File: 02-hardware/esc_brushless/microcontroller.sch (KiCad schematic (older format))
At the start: 0 parts

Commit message: Schematics v1.0 - Architecture, MOS power stage, mos driver stage and RS485 interface
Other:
- note added: "1 I2C"
- note added: "1 SPI"
- note added: "1 input capture"
- note added: "2 UART"
- note added: "4 GPIO input"
- note added: "5 GPIO output"
- note added: "6 timer channels"
- note added: "ADC 7 channels"
- note added: "SWD"
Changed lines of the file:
@@
 $Descr A4 11693 8268
 encoding utf-8
-Sheet 3 5
+Sheet 4 7
 Title "ESC Brushless - Microcontroller"
 Date "2021-02-09"
@@
 Comment4 ""
 $EndDescr
+Text HLabel 2150 5150 0    50   Input ~ 0
+\OVR_CUR_FLT
+Text HLabel 2150 5250 0    50   Input ~ 0
+\FLT
+Text HLabel 950  1600 0    50   UnSpc ~ 0
+3.3V_MCU
+Text HLabel 2150 5050 0    50   Input ~ 0
+\PWRGD_FLT
+Text HLabel 2150 3550 0    50   Output ~ 0
+SPI_CS
+Text HLabel 2150 3650 0    50   Output ~ 0
+SPI_MOSI
+Text HLabel 2150 3850 0    50   Output ~ 0
+SPI_CLK
+Text HLabel 2150 3750 0    50   Input ~ 0
+SPI_MISO
+Text HLabel 2150 4150 0    50   Output ~ 0
+INH_A
+Text HLabel 2150 4250 0    50   Output ~ 0
+INL_A
+Text HLabel 2150 4350 0    50   Output ~ 0
+INH_B
+Text HLabel 2150 4450 0    50   Output ~ 0
+INL_B
+Text HLabel 2150 4550 0    50   Output ~ 0
+INH_C
+Text HLabel 2150 4650 0    50   Output ~ 0
+INL_C
+Text HLabel 2150 1150 0    50   Input ~ 0
+SO1
+Text HLabel 1000 1450 0    50   UnSpc ~ 0
+REF
+Text HLabel 2150 1250 0    50   Input ~ 0
+SO2
+Text HLabel 2150 5700 0    50   Output ~ 0
+DC_CAL
+Text HLabel 2150 5600 0    50   Output ~ 0
+EN_GATE
+Text HLabel 2150 1050 0    50   Input ~ 0
+ADC_C
+Text HLabel 2150 950  0    50   Input ~ 0
+ADC_B
+Text HLabel 2150 850  0    50   Input ~ 0
+ADC_A
+Text HLabel 2150 2250 0    50   Input ~ 0
+UART_RX
+Text HLabel 2150 2750 0    50   Input ~ 0
+I2C_SDA
+Text HLabel 2150 2850 0    50   Input ~ 0
+I2C_SCL
+Text HLabel 2150 4750 0    50   Input ~ 0
+PWM_IN
+Text HLabel 2150 1750 0    50   Input ~ 0
+SW_CLK
+Text HLabel 2150 1850 0    50   Input ~ 0
+SW_DIO
+Text HLabel 2150 1350 0    50   Input ~ 0
+TEMP_SENSOR
+Text HLabel 2150 1450 0    50   Input ~ 0
+ADC_PVDD
+Text HLabel 2150 5800 0    50   Output ~ 0
+LED
+Text HLabel 2150 5350 0    50   Input ~ 0
+\TEST
+Text Notes 2400 1200 0    118  ~ 0
+ADC 7 channels
+Text Notes 2400 1850 0    118  ~ 0
+SWD
+Text Notes 2400 2400 0    118  ~ 0
+2 UART
+Text Notes 2400 2850 0    118  ~ 0
+1 I2C
+Text HLabel 2150 2350 0    50   Output ~ 0
+UART_DEBUG_TX
+Text HLabel 2150 2450 0    50   Input ~ 0
+UART_DEBUG_RX
+Text Notes 2400 3750 0    118  ~ 0
+1 SPI
+Text Notes 2400 4500 0    118  ~ 0
+6 timer channels
+Text Notes 2400 4700 0    118  ~ 0
+1 input capture
+Text Notes 2400 5250 0    118  ~ 0
+4 GPIO input
+Text Notes 2400 5800 0    118  ~ 0
+5 GPIO output
+Text HLabel 2150 5900 0    50   Output ~ 0
+\RS485_RE
+Text HLabel 2150 6000 0    50   Output ~ 0
+RS485_DE
+Text HLabel 2150 2150 0    50   Output ~ 0
+UART_TX
 $EndSCHEMATC

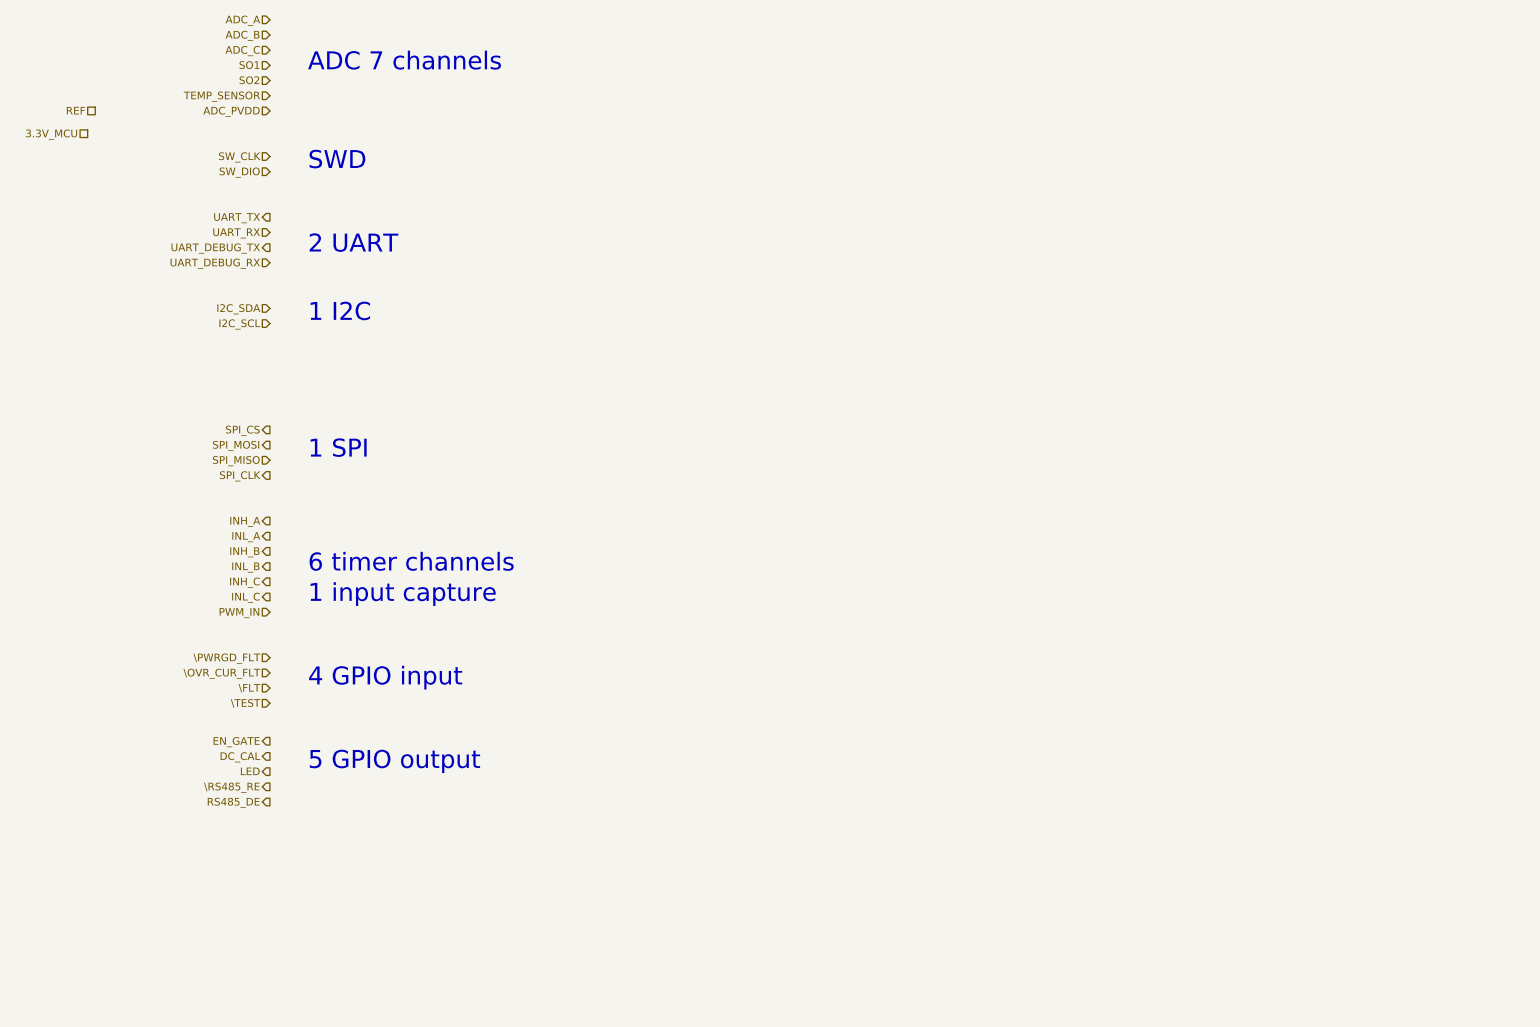
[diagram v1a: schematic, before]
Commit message: Schematics v1.0 - Architecture, microcontroler, global interconnections and IO
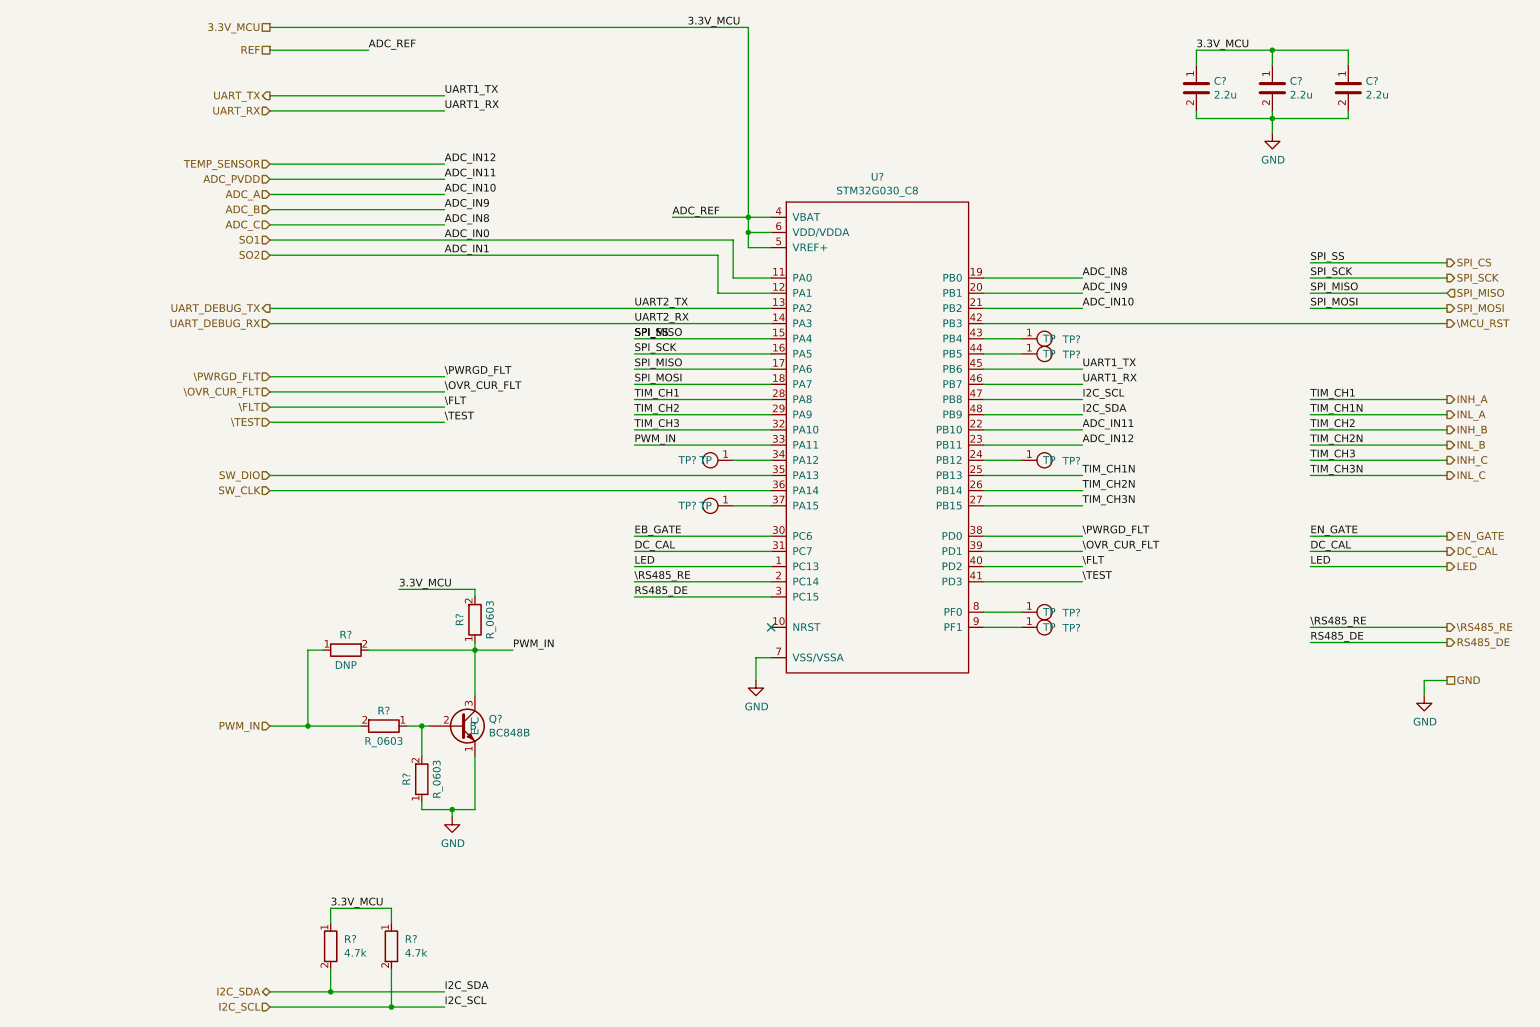
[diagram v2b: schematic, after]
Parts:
- added C? (x3): 2.2u, p_Package_Capacitor_SMD:C_0603_1608Metric_Pad1.08x0.95mm_HandSolder, symbol p_Passive:C_0603
- added Q?: BC848B, p_Package_SOT:SOT-23, symbol p_Transistor_bipolar:BC848B
- added R? (x2): 4.7k, p_Package_Resistor_SMD:R_0603_1608Metric_Pad0.98x0.95mm_HandSolder, symbol p_Passive:R_0603
- added R?: DNP, p_Package_Resistor_SMD:R_0603_1608Metric_Pad0.98x0.95mm_HandSolder, symbol p_Passive:R_0603
- added R? (x3): R_0603, p_Package_Resistor_SMD:R_0603_1608Metric_Pad0.98x0.95mm_HandSolder, symbol p_Passive:R_0603
- added TP? (x7): test_point, p_Package_Misc:TP_SMD_1.25mm, symbol p_Misc:test_point
- added U?: STM32G030_C8, p_Package_QFP:LQFP-48_7x7mm_P0.5mm, symbol p_MCU:STM32G030_C8
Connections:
- net 3.3V_MCU: now also C?.1, C?.1, C?.1, R?.1, R?.1, R?.2, U?.4 (VBAT), U?.5 (VREF+), U?.6 (VDD/VDDA)
- net ADC_A: now also U?.21 (PB2)
- net ADC_B: now also U?.20 (PB1)
- net ADC_C: now also U?.19 (PB0)
- net ADC_PVDD: now also U?.22 (PB10)
- net DC_CAL: now also U?.31 (PC7)
- net I2C_SCL: now also R?.2, U?.47 (PB8)
- net I2C_SDA: now also R?.2, U?.48 (PB9)
- net INH_A: now also U?.28 (PA8)
- net INH_B: now also U?.29 (PA9)
- net INH_C: now also U?.32 (PA10)
- net INL_A: now also U?.25 (PB13)
- net INL_B: now also U?.26 (PB14)
- net INL_C: now also U?.27 (PB15)
- net LED: now also U?.1 (PC13)
- net PWM_IN: now also Q?.3 (C), R?.1, R?.1, R?.2, R?.2, U?.33 (PA11)
- net RS485_DE: now also U?.3 (PC15)
- net SO1: now also U?.11 (PA0)
- net SO2: now also U?.12 (PA1)
- net SPI_CS: now also U?.15 (PA4), U?.17 (PA6)
- net SPI_MOSI: now also U?.18 (PA7)
- net SW_CLK: now also U?.36 (PA14)
- net SW_DIO: now also U?.35 (PA13)
- net TEMP_SENSOR: now also U?.23 (PB11)
- net UART_DEBUG_RX: now also U?.14 (PA3)
- net UART_DEBUG_TX: now also U?.13 (PA2)
- net UART_RX: now also U?.46 (PB7)
- net UART_TX: now also U?.45 (PB6)
- net \FLT: now also U?.40 (PD2)
- net \OVR_CUR_FLT: now also U?.39 (PD1)
- net \PWRGD_FLT: now also U?.38 (PD0)
- net \RS485_RE: now also U?.2 (PC14)
- net \TEST: now also U?.41 (PD3)
- new net: TP?.1 (TP), U?.24 (PB12)
- new net: TP?.1 (TP), U?.34 (PA12)
- new net: TP?.1 (TP), U?.37 (PA15)
- new net: TP?.1 (TP), U?.43 (PB4)
- new net: TP?.1 (TP), U?.44 (PB5)
- new net: TP?.1 (TP), U?.8 (PF0)
- new net: TP?.1 (TP), U?.9 (PF1)
- new net: Q?.2 (B), R?.1, R?.2
- new net EB_GATE: U?.30 (PC6)
- new net GND: C?.2, C?.2, C?.2, Q?.1 (E), R?.1, U?.7 (VSS/VSSA)
- new net SPI_SCK: U?.16 (PA5)
- new net \MCU_RST: U?.42 (PB3)
- no-connect marks 0 -> 1
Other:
- note removed: "1 I2C"
- note removed: "1 SPI"
- note removed: "1 input capture"
- note removed: "2 UART"
- note removed: "4 GPIO input"
- note removed: "5 GPIO output"
- note removed: "6 timer channels"
- note removed: "ADC 7 channels"
- note removed: "SWD"
